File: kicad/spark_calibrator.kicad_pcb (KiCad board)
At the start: 2 copper layers, 60 x 77.8 mm, 18 parts, among them J1 PWM, J2 Coil+, J3 Coil-, J4 12V IN, Q1 BS170, Q2 IRFP460PBF, U1 4N28

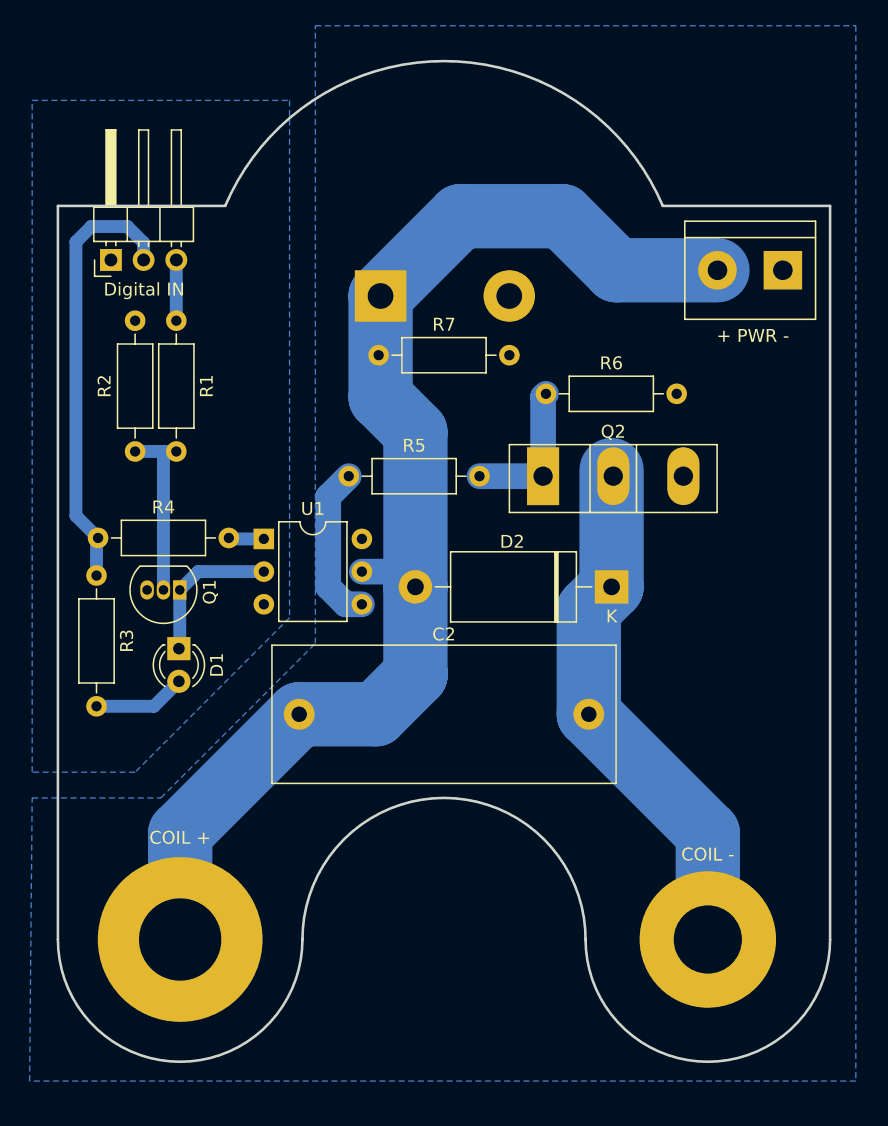
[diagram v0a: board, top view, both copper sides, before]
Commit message: faster off switching
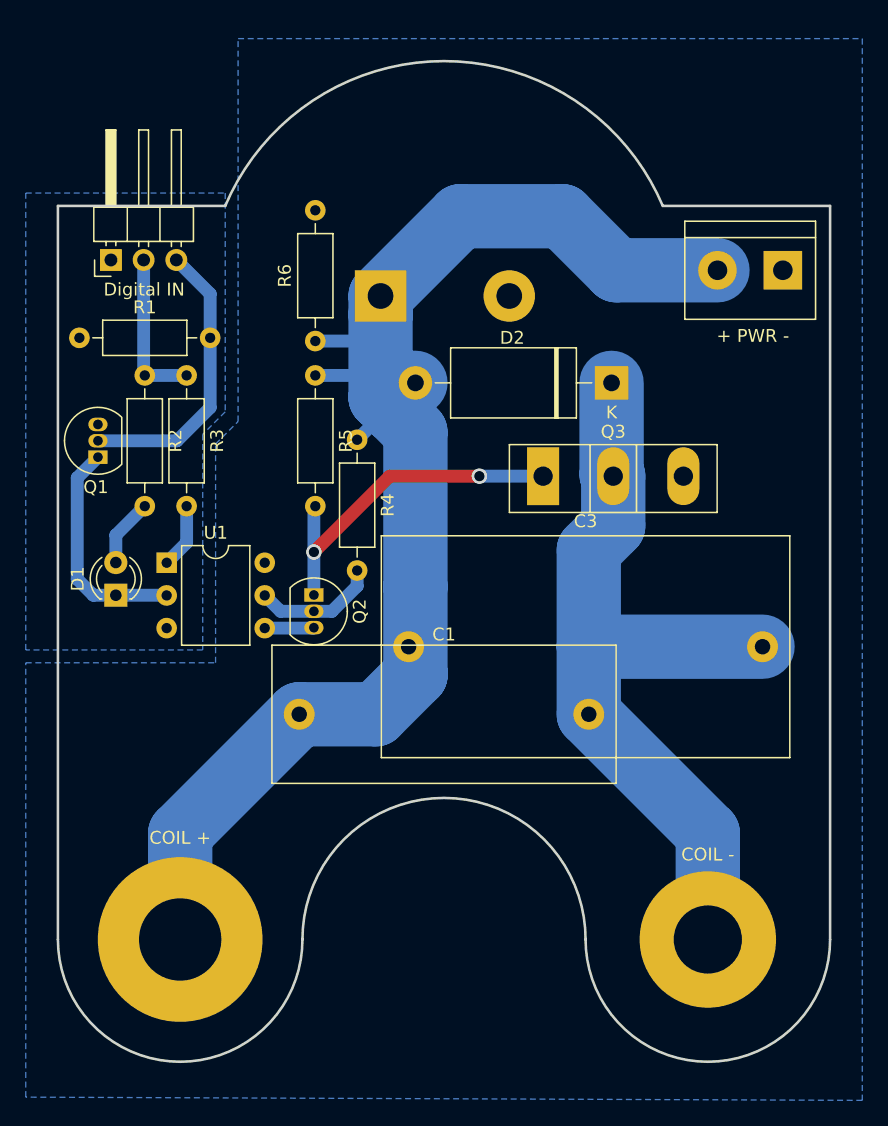
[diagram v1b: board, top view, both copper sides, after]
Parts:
- removed the R2 at (126.0, 87.1)
- added C3: 4.7u 630V, Capacitor_THT:C_Rect_L31.5mm_W17.0mm_P27.50mm_MKS4, F.Cu at (147.2, 102.2)
- added Q2: BS170, Package_TO_SOT_THT:TO-92_Inline, F.Cu at (139.9, 98.2)
- R1: value 100 -> 1k
- R3: renamed from R4; value 220 -> 330
- R5: value 100 -> 2.2k
- moved R2 16.0 mm to (126.8, 81.2)
- moved D2 15.8 mm to (163.0, 81.8)
- moved R4 15.1 mm to (143.2, 86.2), turned to -90 degrees
- moved R3 14.4 mm to (130.0, 81.2), turned to -90 degrees
- moved Q1 12.1 mm to (123.1, 87.5), turned to 90 degrees
- moved R5 8.25 mm to (140.0, 81.2), turned to -90 degrees
- moved U1 7.77 mm to (128.4, 95.7)
- moved R1 7.65 mm to (121.7, 78.2), turned to 0 degrees
- moved D1 6.42 mm to (124.5, 98.2), turned to 90 degrees
- moved R6 5.04 mm to (140.0, 78.5), turned to 90 degrees
- renumbered C2 to C1, C1 to C2, Q2 to Q3, R3 to R2, R6 to R4, R7 to R6
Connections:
- net +3V3 renamed +5VD
- Q1 pad 2: Net-(Q1-Pad2) -> Net-(J1-Pad3)
- R1 pad 1: Net-(J1-Pad3) -> GNDD
- R1 pad 2: Net-(Q1-Pad2) -> Net-(J1-Pad3)
- R4 pad 1: Net-(Q2-Pad1) -> +12V
- R4 pad 2: GND -> Net-(Q2-Pad2)
- R5 pad 1: Net-(R5-Pad1) -> +12V
- U1 pad 4: Net-(R5-Pad1) -> GND
- U1 pad 5: +12V -> Net-(Q2-Pad2)
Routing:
- net +5VD: track 34.3 -> 12.3 mm
- net Net-(C1-Pad2): track 41.0 -> 61.4 mm
- net Net-(J1-Pad3): track 4.72 -> 22.3 mm
- net +12V: track 97.3 -> 113.1 mm
- net Net-(Q2-Pad1): track 11.4 -> 27.2 mm, vias 0 -> 2
- net Net-(Q1-Pad2): track 14.0 -> 0.00 mm
- net Net-(R5-Pad1): track 12.4 -> 0.00 mm
- net Net-(Q2-Pad2): track 0.00 -> 9.72 mm
- net Net-(D1-Pad1): track 11.7 -> 17.6 mm
- net GND: track 0.00 -> 3.83 mm
- net Net-(R3-Pad2): track 2.75 -> 5.04 mm
- net Net-(D1-Pad2): track 7.20 -> 5.31 mm

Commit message: first prototype
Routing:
- net Net-(D1-Pad1): track 17.6 -> 16.2 mm
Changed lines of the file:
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@@
     (pad_to_mask_clearance 0)
     (pcbplotparams
-      (layerselection 0x00010fc_ffffffff)
+      (layerselection 0x0001000_fffffffe)
       (disableapertmacros false)
-      (usegerberextensions false)
+      (usegerberextensions true)
       (usegerberattributes true)
-      (usegerberadvancedattributes true)
+      (usegerberadvancedattributes false)
       (creategerberjobfile true)
       (svguseinch false)
@@
       (plotinvisibletext false)
       (sketchpadsonfab false)
-      (subtractmaskfromsilk false)
+      (subtractmaskfromsilk true)
       (outputformat 1)
       (mirror false)
-      (drillshape 1)
+      (drillshape 0)
       (scaleselection 1)
-      (outputdirectory "")
+      (outputdirectory "gerbers/")
     )
   )
@@
   (segment (start 139.855 100.805) (end 139.89 100.77) (width 1) (layer "B.Cu") (net 8))
   (segment (start 136.07 100.805) (end 139.855 100.805) (width 1) (layer "B.Cu") (net 8))
-  (segment (start 121.5 97) (end 121.5 89.13) (width 1) (layer "B.Cu") (net 9))
-  (segment (start 124.5 98.25) (end 122.75 98.25) (width 1) (layer "B.Cu") (net 9))
+  (segment (start 122.5 97) (end 122.5 88.13) (width 1) (layer "B.Cu") (net 9))
   (segment (start 128.435 98.25) (end 128.45 98.265) (width 1) (layer "B.Cu") (net 9))
+  (segment (start 123.75 98.25) (end 122.5 97) (width 1) (layer "B.Cu") (net 9))
+  (segment (start 122.5 88.13) (end 123.11 87.52) (width 1) (layer "B.Cu") (net 9))
   (segment (start 124.5 98.25) (end 128.435 98.25) (width 1) (layer "B.Cu") (net 9))
-  (segment (start 122.75 98.25) (end 121.5 97) (width 1) (layer "B.Cu") (net 9))
-  (segment (start 121.5 89.13) (end 123.11 87.52) (width 1) (layer "B.Cu") (net 9))
+  (segment (start 124.5 98.25) (end 123.75 98.25) (width 1) (layer "B.Cu") (net 9))
   (segment (start 161.25 102.25) (end 161.25 94.75) (width 5) (layer "B.Cu") (net 12))
   (segment (start 170.5 125) (end 170.5 116.75) (width 5) (layer "B.Cu") (net 12))
@@
   (segment (start 157.7 89) (end 152.75 89) (width 1) (layer "B.Cu") (net 13))
   (zone (net 8) (net_name "GND") (layer "B.Cu") (hatch edge 0.508)
-    (connect_pads (clearance 1))
+    (connect_pads (clearance 0.508))
     (min_thickness 0.254) (filled_areas_thickness no)
     (fill yes (thermal_gap 0.508) (thermal_bridge_width 0.508))
